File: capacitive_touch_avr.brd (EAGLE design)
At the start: 24.1 x 46 mm, 10 parts, among them J2 JACK-2.1MM

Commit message: The same as last commit but deleting via and pad for further modifications
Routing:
- net N$1: track 5.98 -> 0.00 mm, vias 1 -> 0
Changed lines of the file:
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@@
 <dimension x1="24.11" y1="46.025" x2="0" y2="46.025" x3="12.055" y3="48.26" textsize="1.778" layer="20"/>
 <dimension x1="0" y1="46.025" x2="0" y2="0" x3="-3.175" y3="23.0125" textsize="1.778" layer="20"/>
-<circle x="12.065" y="31.115" radius="7.62" width="0.1524" layer="16"/>
 </plain>
 <attributes>
@@
 <wire x1="12.7" y1="23.241" x2="16.51" y2="23.241" width="0.4064" layer="1"/>
 </signal>
-<signal name="N$1">
-<via x="12.7" y="25.4" extent="1-16" drill="0.55"/>
-<wire x1="12.7" y1="25.4" x2="12.065" y2="26.035" width="0.4064" layer="16"/>
-<wire x1="12.065" y1="26.035" x2="12.065" y2="31.115" width="0.4064" layer="16"/>
-</signal>
 </signals>

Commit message: Version 1. Touch pad + full wiring
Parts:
- added ESD-C3: 0.1uF, fab:C1206FAB
- moved U$3 29.9 mm to (23.5, 6.99)
- moved U$4 26.7 mm to (3.81, 15.9), turned to 90 degrees
- moved R2 14.7 mm to (3.81, 6.99), turned to 90 degrees
- moved U$1 9.61 mm to (13.3, 21.6)
- moved C2 7.65 mm to (17.8, 15.9)
- moved R4 7.65 mm to (21.6, 15.9)
- moved R3 7.24 mm to (24.8, 15.9)
- moved R1 5.75 mm to (8.26, 15.9)
- moved C1 2.29 mm to (13.3, 14.6)
- moved J2 1.27 mm to (13.3, 5.71)
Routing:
- net VCC: track 72.6 -> 53.0 mm
- net N$3: track 5.59 -> 21.1 mm
- net CPIN: track 8.53 -> 23.8 mm, vias 0 -> 1
- net MOSI: track 6.16 -> 15.4 mm
- net GND: track 71.7 -> 76.1 mm
- net N$4: track 7.11 -> 5.23 mm
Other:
- board size 24.1 x 46 mm -> 27.3 x 47.9 mm

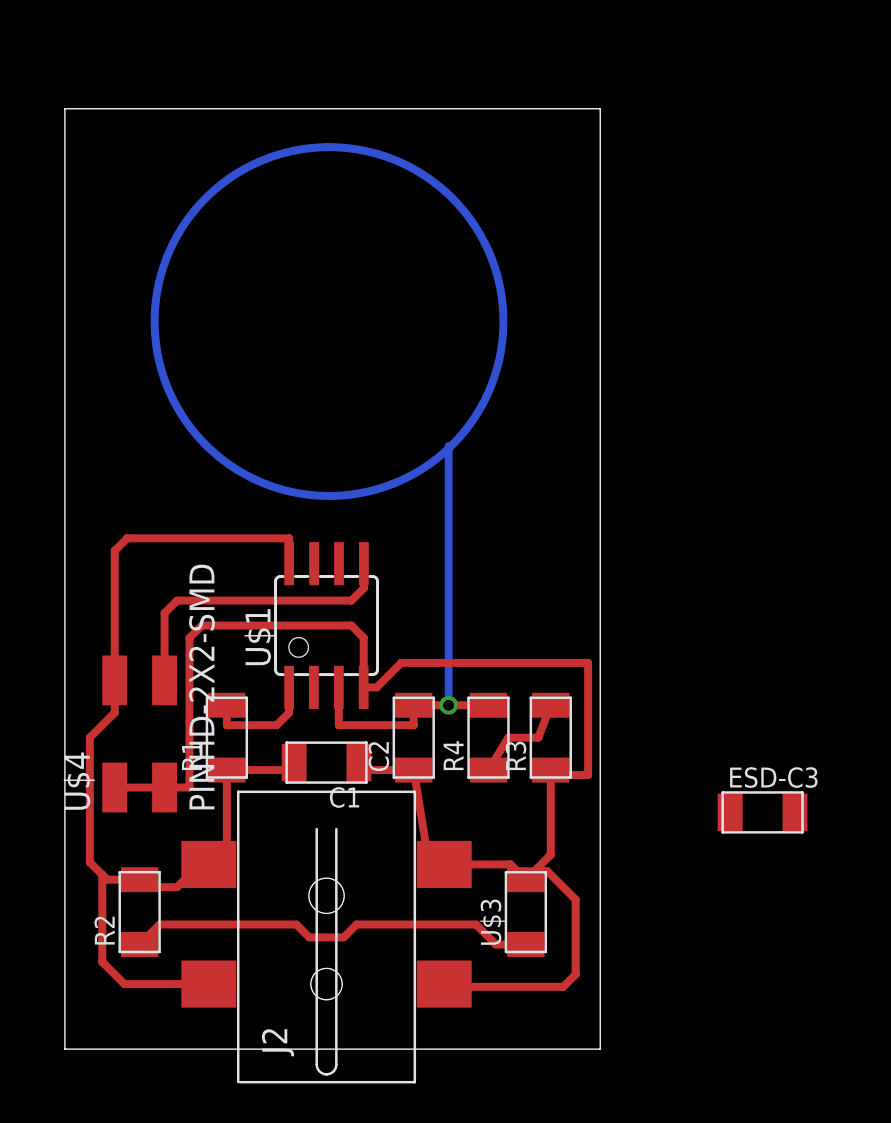
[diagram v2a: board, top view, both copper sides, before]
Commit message: Version 2.0 isolate signals from sensor pin + pad design Missing ESD shield + Mounting holes
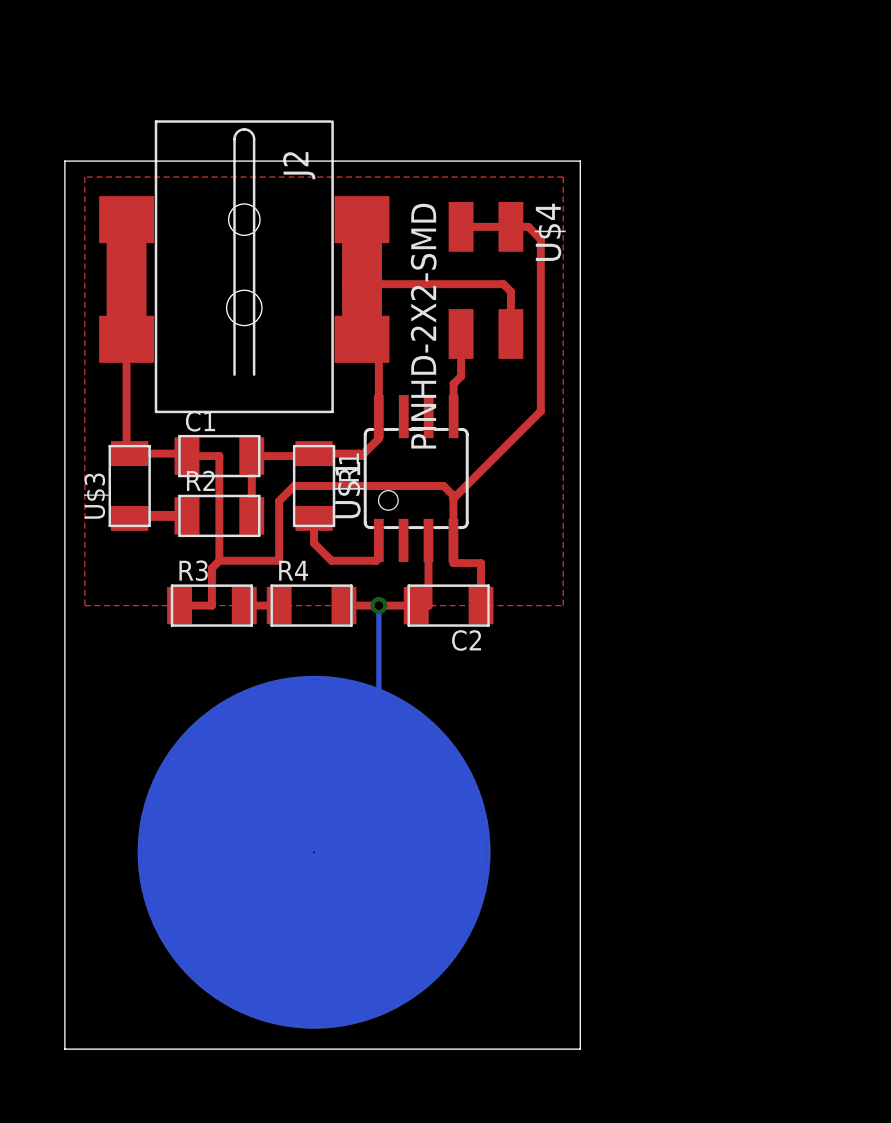
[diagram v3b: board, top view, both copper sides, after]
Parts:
- removed ESD-C3: 0.1uF, fab:C1206FAB
- moved J2 34.4 mm to (9.14, 39.9), turned to 270 degrees
- moved U$3 29.7 mm to (3.30, 28.7)
- moved U$4 29.4 mm to (21.5, 39.4), turned to 270 degrees
- moved R2 20.6 mm to (7.87, 27.2), turned to 0 degrees
- moved R3 18.5 mm to (7.49, 22.6), turned to 0 degrees
- moved C1 16.5 mm to (7.87, 30.2), turned to 0 degrees
- moved R1 13.6 mm to (12.7, 28.7), turned to 270 degrees
- moved R4 11.3 mm to (12.6, 22.6), turned to 0 degrees
- moved U$1 8.78 mm to (17.9, 29.1)
- moved C2 6.96 mm to (19.6, 22.6), turned to 180 degrees
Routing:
- net VCC: track 53.0 -> 32.1 mm
- net N$3: track 21.1 -> 2.97 mm
- net CPIN: track 23.8 -> 12.5 mm
- net MOSI: track 15.4 -> 4.37 mm
- net GND: track 76.1 -> 69.1 mm
- net N$4: track 5.23 -> 1.78 mm
- added copper zone on layer 1, net GND
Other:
- board size 27.3 x 47.9 mm -> 26.3 x 45.3 mm

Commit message: Adding ISP and jumber at sensor R
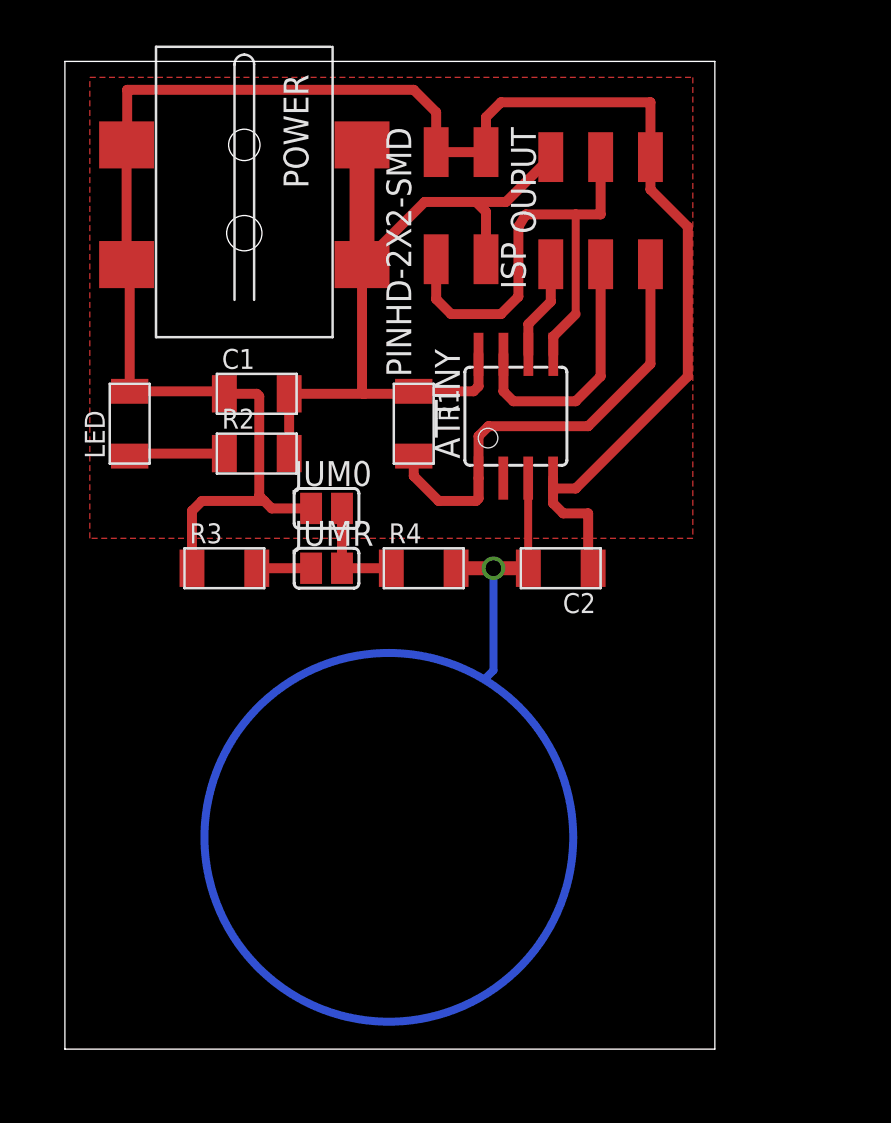
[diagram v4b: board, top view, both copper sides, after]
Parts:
- removed J2: JACK-2.1MM, fab:PJ-002AH-SMT
- removed U$1: ATTINY45SI, fab:SOIC8
- removed U$3: LEDFAB1206, fab:LED1206FAB
- removed U$4: PINHD-2X2-SMD, fab:2X02SMD
- added ATTINY: ATTINY45SI, fab:SOIC8
- added ISP: AVRISPSMD, fab:2X03SMD
- added JUM0, JUMR: SOLDER_JUMPER, fab:SJFAB
- added LED: LEDFAB1206, fab:LED1206FAB
- added OUPUT: PINHD-2X2-SMD, fab:2X02SMD
- added POWER: JACK-2.1MM, fab:PJ-002AH-SMT
- moved C2 6.02 mm to (25.3, 24.5)
- moved R4 6.02 mm to (18.3, 24.5)
- moved R1 5.99 mm to (17.8, 31.9)
- moved C1 3.70 mm to (9.78, 33.4)
- moved R2 3.70 mm to (9.78, 30.4)
- moved R3 2.01 mm to (8.13, 24.5)
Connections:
- removed net N$4: R3.2, R4.1
- new net N$1: JUM0.2, JUMR.2, R4.1
- new net N$2: JUMR.1, R3.2
- net CPIN: now also ATTINY.3; no longer U$1.3
- net GND: now also ATTINY.4, ISP.6, JUM0.1, LED.2, OUPUT.1, OUPUT.3, POWER.CONTACT, POWER.SHUNT; no longer J2.CONTACT, J2.SHUNT, U$1.4, U$3.2, U$4.1, U$4.3
- net MISO: now also ATTINY.6, ISP.1; no longer U$1.6
- net MOSI: now also ATTINY.5, ISP.4, OUPUT.4; no longer U$1.5, U$4.4
- net N$3: now also LED.1; no longer U$3.1
- net RST: now also ATTINY.1, ISP.5; no longer U$1.1
- net SCK: now also ATTINY.7, ISP.3; no longer U$1.7
- net VCC: now also ATTINY.8, ISP.2, OUPUT.2, POWER.PIN1, POWER.PIN2; no longer J2.PIN1, J2.PIN2, U$1.8, U$4.2
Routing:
- net GND: track 69.1 -> 100.1 mm
- net MOSI: track 4.37 -> 25.5 mm
- net RST: track 5.90 -> 23.4 mm
- net SCK: track 0.00 -> 13.3 mm
- net VCC: track 32.1 -> 42.7 mm
- net N$1: track 0.00 -> 5.56 mm
- net MISO: track 0.00 -> 5.07 mm
- net N$2: track 0.00 -> 2.77 mm
- net N$3: track 2.97 -> 4.88 mm
- net N$4: track 1.78 -> 0.00 mm
- net CPIN: track 12.5 -> 14.0 mm
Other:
- board size 26.3 x 45.3 mm -> 33.1 x 50.3 mm

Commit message: Tested and working version Modifying power jack from SMD to TH
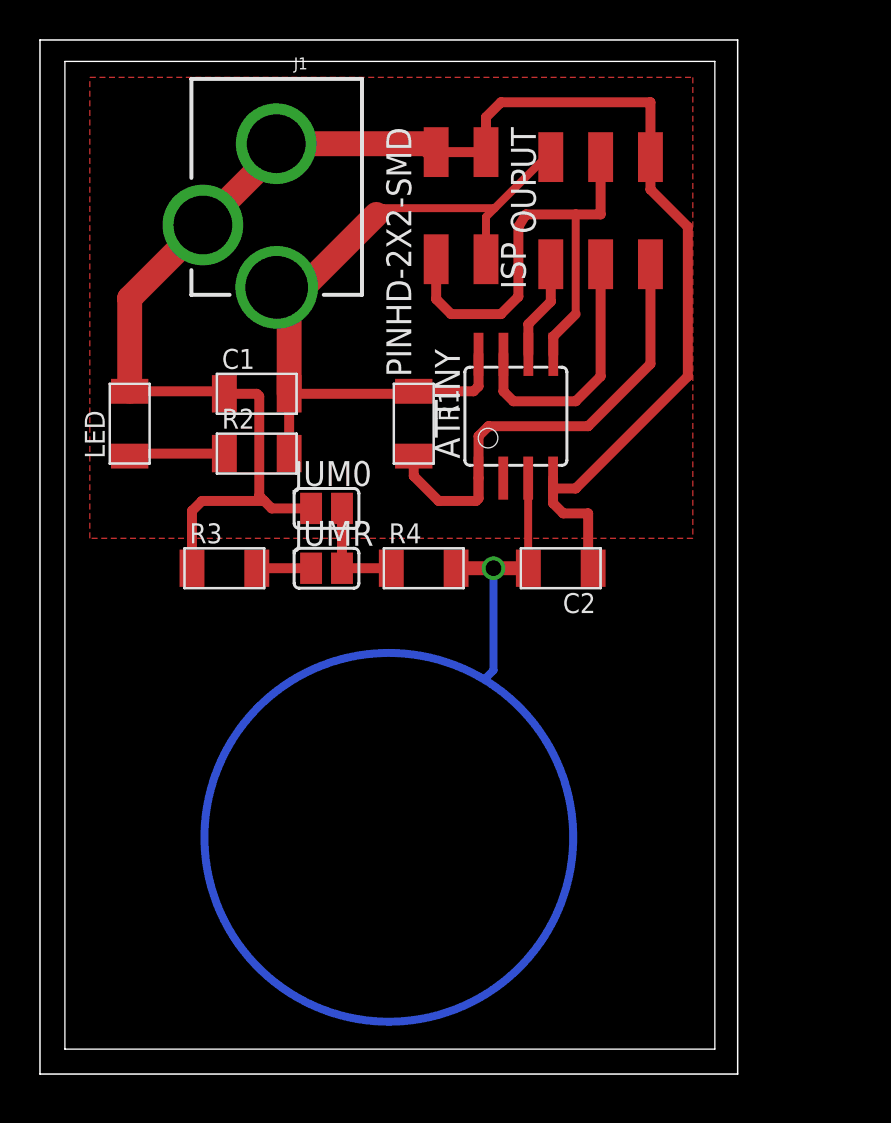
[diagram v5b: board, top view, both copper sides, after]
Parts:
- removed POWER: JACK-2.1MM, fab:PJ-002AH-SMT
- added J1: POWER_JACKPTH_LOCK, SparkFun-Connectors:POWER_JACK_PTH_LOCK
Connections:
- net GND: now also J1.GND, J1.GNDBREAK; no longer POWER.CONTACT, POWER.SHUNT
- net VCC: now also J1.PWR; no longer POWER.PIN1, POWER.PIN2
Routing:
- net GND: track 100.1 -> 88.7 mm
- net VCC: track 42.7 -> 39.7 mm
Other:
- board size 33.1 x 50.3 mm -> 35.6 x 52.7 mm
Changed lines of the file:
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@@
 <drawing>
 <settings>
-<setting alwaysvectorfont="yes"/>
+<setting alwaysvectorfont="no"/>
 <setting verticaltext="up"/>
 </settings>
@@
 <layer number="25" name="tNames" color="7" fill="1" visible="yes" active="yes"/>
 <layer number="26" name="bNames" color="7" fill="1" visible="yes" active="yes"/>
-<layer number="27" name="tValues" color="7" fill="1" visible="yes" active="yes"/>
-<layer number="28" name="bValues" color="7" fill="1" visible="yes" active="yes"/>
+<layer number="27" name="tValues" color="7" fill="1" visible="no" active="yes"/>
+<layer number="28" name="bValues" color="7" fill="1" visible="no" active="yes"/>
 <layer number="29" name="tStop" color="7" fill="3" visible="no" active="yes"/>
 <layer number="30" name="bStop" color="7" fill="6" visible="no" active="yes"/>
@@
 <layer number="230" name="230bmp" color="7" fill="1" visible="no" active="yes"/>
 <layer number="231" name="231bmp" color="7" fill="1" visible="no" active="yes"/>
+<layer number="232" name="Eagle3D_PG2" color="7" fill="1" visible="no" active="yes"/>
+<layer number="233" name="Eagle3D_PG3" color="7" fill="1" visible="no" active="yes"/>
 <layer number="248" name="Housing" color="7" fill="1" visible="no" active="yes"/>
 <layer number="249" name="Edge" color="7" fill="1" visible="no" active="yes"/>
@@
 <wire x1="0" y1="50.343" x2="0" y2="0" width="0" layer="20"/>
 <circle x="16.51" y="10.795" radius="9.398" width="0.4064" layer="16"/>
+<wire x1="-1.27" y1="-1.27" x2="34.29" y2="-1.27" width="0.0762" layer="20"/>
+<wire x1="34.29" y1="-1.27" x2="34.29" y2="51.435" width="0.0762" layer="20"/>
+<wire x1="34.29" y1="51.435" x2="-1.27" y2="51.435" width="0.0762" layer="20"/>
+<wire x1="-1.27" y1="51.435" x2="-1.27" y2="-1.27" width="0.0762" layer="20"/>
 </plain>
 <attributes>
@@
 </element>
 <element name="OUPUT" library="fab" package="2X02SMD" value="PINHD-2X2-SMD" x="20.193" y="43.18" rot="R270"/>
-<element name="POWER" library="fab" package="PJ-002AH-SMT" value="JACK-2.1MM" x="9.144" y="43.688" rot="R270"/>
 <element name="ISP" library="fab" package="2X03SMD" value="AVRISPSMD" x="27.305" y="42.545" rot="R90"/>
 <element name="JUMR" library="fab" package="SJFAB" value="SOLDER_JUMPER" x="13.335" y="24.511"/>
 <element name="JUM0" library="fab" package="SJFAB" value="SOLDER_JUMPER" x="13.335" y="27.559"/>
+<element name="J1" library="SparkFun-Connectors" library_urn="urn:adsk.eagle:library:513" package="POWER_JACK_PTH_LOCK" package3d_urn="urn:adsk.eagle:package:38224/1" value="POWER_JACKPTH_LOCK" x="10.795" y="52.705" rot="R180">
+<attribute name="PROD_ID" value="CONN-08197" x="10.795" y="52.705" size="1.778" layer="27" rot="R180" display="off"/>
+<attribute name="SF_ID" value="PRT-00119" x="10.795" y="52.705" size="1.778" layer="27" rot="R180" display="off"/>
+</element>
 </elements>
 <signals>
@@
 <contactref element="R2" pad="2"/>
 <contactref element="OUPUT" pad="2"/>
-<contactref element="POWER" pad="PIN1"/>
-<contactref element="POWER" pad="PIN2"/>
 <contactref element="ISP" pad="2"/>
-<wire x1="15.24" y1="45.72" x2="15.144" y2="46.088" width="0.1524" layer="1"/>
-<wire x1="18.336" y1="43.18" x2="15.144" y2="39.988" width="0.508" layer="1"/>
-<wire x1="21.463" y1="40.26" x2="21.463" y2="42.672" width="0.508" layer="1"/>
-<wire x1="21.463" y1="42.672" x2="20.955" y2="43.18" width="0.508" layer="1"/>
-<wire x1="20.955" y1="43.18" x2="18.336" y2="43.18" width="0.508" layer="1"/>
-<wire x1="24.765" y1="45.465" x2="22.48" y2="43.18" width="0.508" layer="1"/>
-<wire x1="22.48" y1="43.18" x2="20.955" y2="43.18" width="0.508" layer="1"/>
 <wire x1="17.78" y1="33.528" x2="20.828" y2="33.528" width="0.508" layer="1"/>
 <wire x1="21.082" y1="33.782" x2="21.082" y2="35.412" width="0.508" layer="1"/>
 <wire x1="20.828" y1="33.528" x2="21.082" y2="33.782" width="0.508" layer="1"/>
-<wire x1="11.43" y1="33.401" x2="15.24" y2="33.401" width="0.508" layer="1"/>
-<wire x1="15.24" y1="33.401" x2="17.653" y2="33.401" width="0.508" layer="1"/>
+<wire x1="11.43" y1="33.401" x2="17.653" y2="33.401" width="0.508" layer="1"/>
 <wire x1="17.653" y1="33.401" x2="17.78" y2="33.528" width="0.508" layer="1"/>
 <wire x1="11.43" y1="30.353" x2="11.43" y2="33.401" width="0.508" layer="1"/>
-<wire x1="15.144" y1="39.988" x2="15.144" y2="33.497" width="0.508" layer="1"/>
-<wire x1="15.144" y1="33.497" x2="15.24" y2="33.401" width="0.508" layer="1"/>
-<wire x1="15.144" y1="46.088" x2="15.144" y2="40.736" width="1.27" layer="1"/>
-<wire x1="15.24" y1="40.005" x2="15.144" y2="40.736" width="0.508" layer="1"/>
-<wire x1="15.144" y1="39.988" x2="15.161" y2="40.005" width="0.508" layer="1"/>
-<wire x1="15.161" y1="40.005" x2="15.24" y2="40.005" width="0.508" layer="1"/>
+<contactref element="J1" pad="PWR"/>
+<wire x1="10.795" y1="38.8272" x2="11.43" y2="38.1922" width="1.27" layer="1"/>
+<wire x1="11.43" y1="38.1922" x2="11.43" y2="33.401" width="1.27" layer="1"/>
+<wire x1="21.463" y1="40.26" x2="21.463" y2="42.418" width="0.4064" layer="1"/>
+<wire x1="24.51" y1="45.465" x2="24.765" y2="45.465" width="0.4064" layer="1"/>
+<wire x1="21.463" y1="42.418" x2="21.9075" y2="42.8625" width="0.4064" layer="1"/>
+<wire x1="21.9075" y1="42.8625" x2="24.51" y2="45.465" width="0.4064" layer="1"/>
+<wire x1="21.9075" y1="42.8625" x2="16.1925" y2="42.8625" width="0.4064" layer="1"/>
+<wire x1="15.875" y1="42.545" x2="16.1925" y2="42.8625" width="0.4064" layer="1"/>
+<wire x1="10.795" y1="38.8272" x2="12.1572" y2="38.8272" width="1.27" layer="1"/>
+<wire x1="12.1572" y1="38.8272" x2="15.875" y2="42.545" width="1.27" layer="1"/>
 </signal>
 <signal name="GND">
@@
 <contactref element="OUPUT" pad="3"/>
 <contactref element="OUPUT" pad="1"/>
-<contactref element="POWER" pad="CONTACT"/>
-<contactref element="POWER" pad="SHUNT"/>
 <contactref element="ISP" pad="6"/>
 <contactref element="JUM0" pad="1"/>
-<wire x1="18.415" y1="45.72" x2="18.923" y2="45.72" width="0.1524" layer="1"/>
 <wire x1="29.845" y1="45.465" x2="29.845" y2="48.26" width="0.508" layer="1"/>
 <wire x1="29.845" y1="48.26" x2="22.225" y2="48.26" width="0.508" layer="1"/>
@@
 <wire x1="3.302" y1="33.528" x2="8.001" y2="33.528" width="0.508" layer="1"/>
 <wire x1="8.001" y1="33.528" x2="8.128" y2="33.401" width="0.508" layer="1"/>
-<wire x1="3.302" y1="33.528" x2="3.302" y2="39.83" width="0.508" layer="1"/>
-<wire x1="3.302" y1="39.83" x2="3.144" y2="39.988" width="0.508" layer="1"/>
 <wire x1="9.906" y1="28.194" x2="9.906" y2="33.274" width="0.508" layer="1"/>
 <wire x1="9.906" y1="33.274" x2="9.779" y2="33.401" width="0.508" layer="1"/>
@@
 <wire x1="24.882" y1="27.823" x2="25.4" y2="27.305" width="0.508" layer="1"/>
 <wire x1="25.4" y1="27.305" x2="26.67" y2="27.305" width="0.508" layer="1"/>
-<wire x1="17.78" y1="48.895" x2="3.175" y2="48.895" width="0.508" layer="1"/>
-<wire x1="3.175" y1="46.119" x2="3.175" y2="48.895" width="0.508" layer="1"/>
-<wire x1="17.78" y1="48.895" x2="18.923" y2="47.752" width="0.508" layer="1"/>
-<wire x1="3.144" y1="46.088" x2="3.144" y2="39.988" width="0.508" layer="1"/>
-<wire x1="3.144" y1="39.974" x2="3" y2="39.83" width="0.508" layer="1"/>
-<wire x1="2.54" y1="39.37" x2="3" y2="39.83" width="0.508" layer="1"/>
-<wire x1="3" y1="39.83" x2="3.302" y2="39.83" width="0.508" layer="1"/>
 <wire x1="29.845" y1="45.465" x2="29.845" y2="43.815" width="0.508" layer="1"/>
 <wire x1="31.75" y1="41.91" x2="31.75" y2="34.29" width="0.508" layer="1"/>
@@
 <wire x1="6.477" y1="27.432" x2="6.985" y2="27.94" width="0.508" layer="1"/>
 <wire x1="6.985" y1="27.94" x2="10.16" y2="27.94" width="0.508" layer="1"/>
-<wire x1="3.144" y1="46.088" x2="3.175" y2="46.119" width="0.508" layer="1"/>
-<wire x1="3.144" y1="39.988" x2="3.144" y2="39.974" width="0.508" layer="1"/>
-<wire x1="18.923" y1="47.752" x2="18.923" y2="45.72" width="0.508" layer="1"/>
 <polygon width="0.4064" layer="1" isolate="0.6096">
 <vertex x="1.27" y="49.53"/>
@@
 <vertex x="1.27" y="26.035"/>
 </polygon>
+<contactref element="J1" pad="GNDBREAK"/>
+<contactref element="J1" pad="GND"/>
+<wire x1="3.302" y1="33.528" x2="3.302" y2="38.2736" width="1.27" layer="1"/>
+<wire x1="3.302" y1="38.2736" x2="7.0334" y2="42.005" width="1.27" layer="1"/>
+<wire x1="7.0334" y1="42.005" x2="10.7696" y2="45.7412" width="1.27" layer="1"/>
+<wire x1="10.7696" y1="45.7412" x2="10.7696" y2="46.148" width="1.27" layer="1"/>
+<wire x1="10.7696" y1="46.148" x2="18.495" y2="46.148" width="1.27" layer="1"/>
+<wire x1="18.495" y1="46.148" x2="18.923" y2="45.72" width="1.27" layer="1"/>
 </signal>
 <signal name="MOSI">
@@
 </drawing>
 <compatibility>
+<note version="8.2" severity="warning">
+Since Version 8.2, EAGLE supports online libraries. The ids
+of those online libraries will not be understood (or retained)
+with this version.
+</note>
 <note version="8.3" severity="warning">
 Since Version 8.3, EAGLE supports Fusion synchronisation.
@@
 the document will break the link to the Fusion PCB feature.
 </note>
+<note version="8.3" severity="warning">
+Since Version 8.3, EAGLE supports URNs for individual library
+assets (packages, symbols, and devices). The URNs of those assets
+will not be understood (or retained) with this version.
+</note>
+<note version="8.3" severity="warning">
+Since Version 8.3, EAGLE supports the association of 3D packages
+with devices in libraries, schematics, and board files. Those 3D
+packages will not be understood (or retained) with this version.
+</note>
 </compatibility>
